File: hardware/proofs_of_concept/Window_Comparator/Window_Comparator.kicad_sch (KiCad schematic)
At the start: 9 parts, among them U1101 LM393

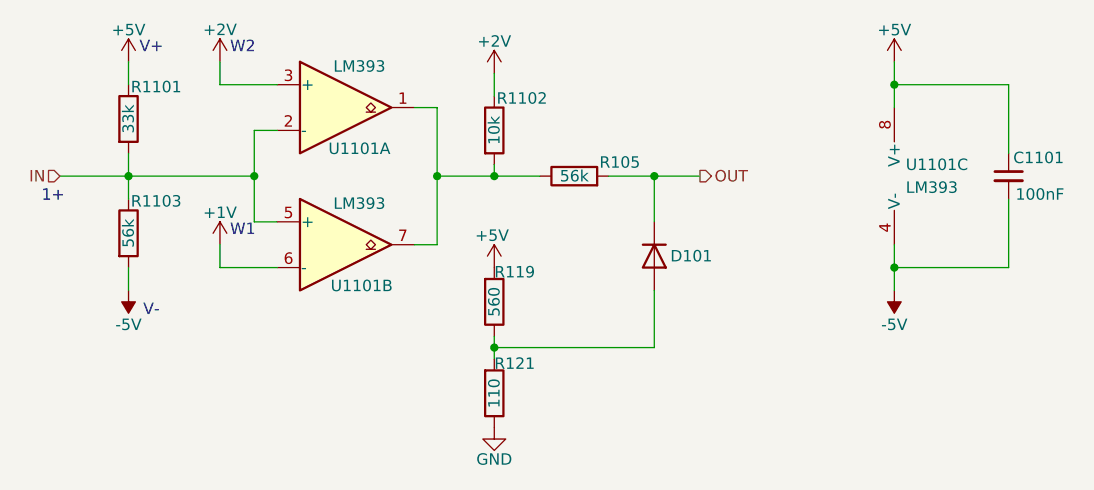
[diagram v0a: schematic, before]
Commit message: Added Window comparator breadboard schematic
Added Cascaded 74xx165 breadboard schematic
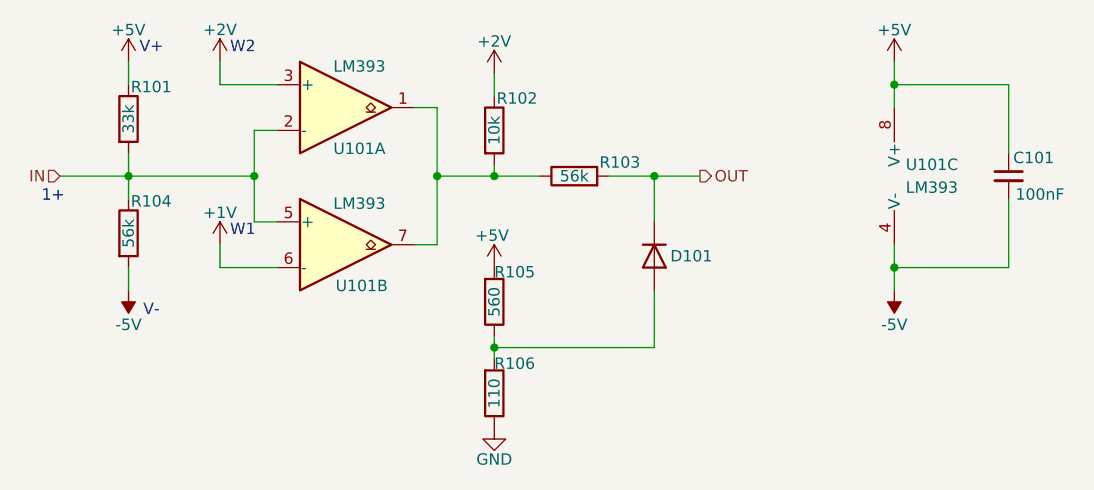
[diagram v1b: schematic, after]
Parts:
- renumbered C1101 to C101, R1101 to R101, R1102 to R102, R105 to R103, R1103 to R104, R119 to R105, R121 to R106, U1101 to U101

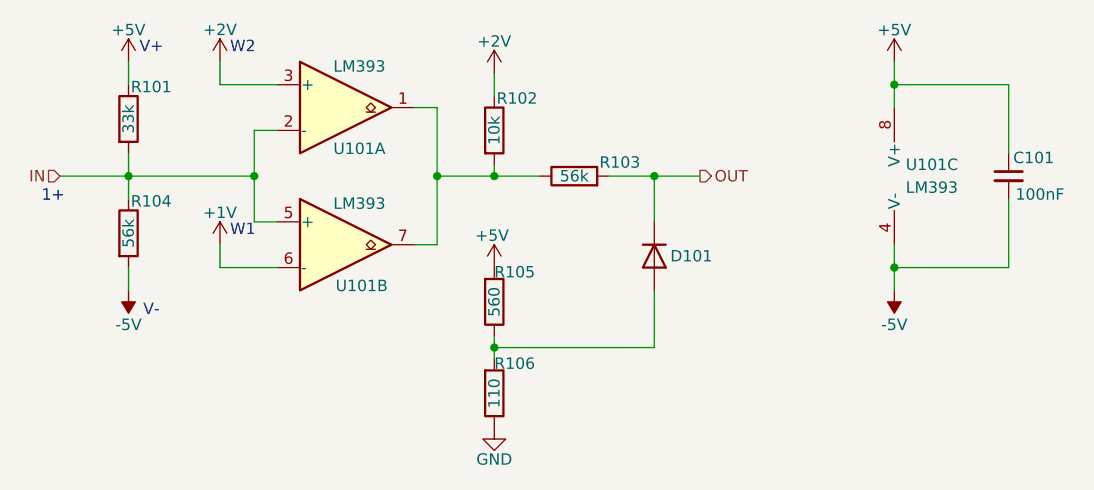
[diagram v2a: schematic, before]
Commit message: Finished proof of concept Window_Comparator and integration test Window_Comparator with Cascaded_74xx165
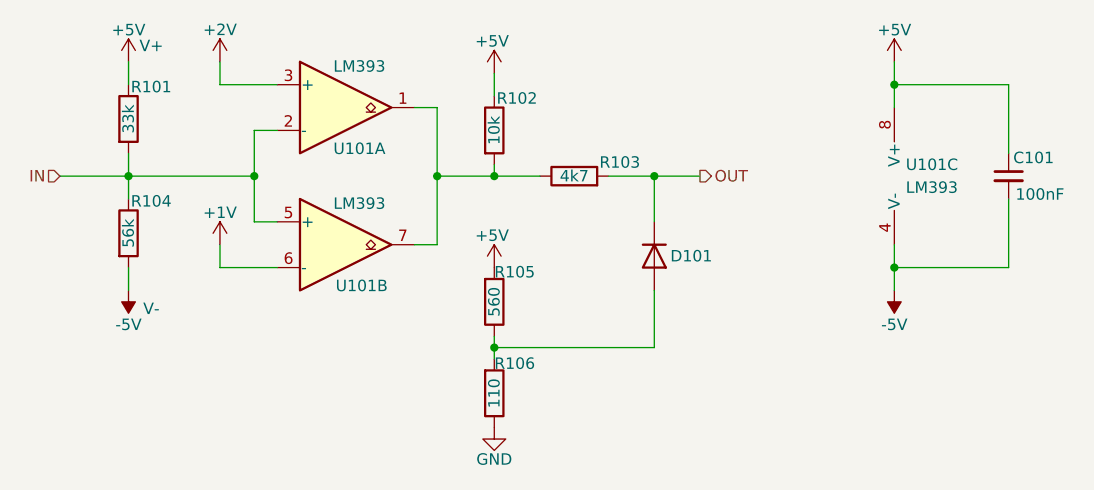
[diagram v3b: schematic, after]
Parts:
- R103: value 56k -> 4k7
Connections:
- net +2V: no longer R102.1
- net +5V: now also R102.1
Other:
- note removed: "1+"
- note removed: "W1"
- note removed: "W2"
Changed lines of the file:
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@@
-		)
-	)
-	(text "1+"
-		(exclude_from_sim no)
-		(at 52.578 68.326 0)
-		(effects
-			(font
-				(size 1.27 1.27)
-			)
-		)
-	)
-	(text "W2"
-		(exclude_from_sim no)
-		(at 73.66 51.816 0)
-		(effects
-			(font
-				(size 1.27 1.27)
-			)
 		)
 	)
@@
 		(exclude_from_sim no)
 		(at 63.5 81.026 0)
-		(effects
-			(font
-				(size 1.27 1.27)
-			)
-		)
-	)
-	(text "W1"
-		(exclude_from_sim no)
-		(at 73.66 72.136 0)
 		(effects
 			(font
@@
 				)
 			)
-			(table_cell "+2V"
+			(table_cell "+5V"
 				(exclude_from_sim no)
 				(at 100.33 110.49 0)
@@
 				)
 			)
-			(table_cell "+2V"
+			(table_cell "+5V"
 				(exclude_from_sim no)
 				(at 100.33 115.57 0)
@@
 	)
 	(symbol
-		(lib_id "power:+5V")
-		(at 101.6 54.61 0)
-		(mirror y)
-		(unit 1)
-		(exclude_from_sim no)
-		(in_bom yes)
-		(on_board yes)
-		(dnp no)
-		(property "Reference" "#PWR0104"
-			(at 101.6 58.42 0)
-			(effects
-				(font
-					(size 1.27 1.27)
-				)
-				(hide yes)
-			)
-		)
-		(property "Value" "+2V"
-			(at 101.6 51.816 0)
-			(effects
-				(font
-					(size 1.27 1.27)
-				)
-				(justify bottom)
-			)
-		)
-		(property "Footprint" ""
-			(at 101.6 54.61 0)
-			(effects
-				(font
-					(size 1.27 1.27)
-				)
-				(hide yes)
-			)
-		)
-		(property "Datasheet" ""
-			(at 101.6 54.61 0)
-			(effects
-				(font
-					(size 1.27 1.27)
-				)
-				(hide yes)
-			)
-		)
-		(property "Description" "Power symbol creates a global label with name \"+5V\""
-			(at 101.6 54.61 0)
-			(effects
-				(font
-					(size 1.27 1.27)
-				)
-				(hide yes)
-			)
-		)
-		(pin "1"
-		)
-		(instances
-			(project "Window_Comparator"
-				(path "/089f60be-ff73-4a85-aea6-2d9ffb548530"
-					(reference "#PWR0104")
-					(unit 1)
-				)
-			)
-		)
-	)
-	(symbol
 		(lib_id "Device:R")
 		(at 101.6 60.96 0)
@@
 			)
 		)
-		(property "Value" "56k"
+		(property "Value" "4k7"
 			(at 110.49 66.04 90)
 			(effects
@@
 					(unit 1)
 				)
+			)
+		)
+	)
+	(symbol
+		(lib_id "power:+5V")
+		(at 101.6 54.61 0)
+		(unit 1)
+		(exclude_from_sim no)
+		(in_bom yes)
+		(on_board yes)
+		(dnp no)
+		(property "Reference" "#PWR0104"
+			(at 101.6 58.42 0)
+			(effects
+				(font
+					(size 1.27 1.27)
+				)
+				(hide yes)
+			)
+		)
+		(property "Value" "+5V"
+			(at 101.346 51.054 0)
+			(effects
+				(font
+					(size 1.27 1.27)
+				)
+			)
+		)
+		(property "Footprint" ""
+			(at 101.6 54.61 0)
+			(effects
+				(font
+					(size 1.27 1.27)
+				)
+				(hide yes)
+			)
+		)
+		(property "Datasheet" ""
+			(at 101.6 54.61 0)
+			(effects
+				(font
+					(size 1.27 1.27)
+				)
+				(hide yes)
+			)
+		)
+		(property "Description" "Power symbol creates a global label with name \"+5V\""
+			(at 101.6 54.61 0)
+			(effects
+				(font
+					(size 1.27 1.27)
+				)
+				(hide yes)
+			)
+		)
+		(pin "1"
+		)
+		(instances
+			(project "Window_Comparator"
+				(path "/089f60be-ff73-4a85-aea6-2d9ffb548530"
+					(reference "#PWR0104")
+					(unit 1)
+				)
